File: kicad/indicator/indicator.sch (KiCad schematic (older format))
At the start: 9 parts, among them J1 Conn_01x03, Q1 2N3904, Q2 2N3904

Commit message: add pcb
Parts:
- D1, D2, D3, D4: footprint (none) -> LED_THT:LED_D3.0mm
- J1: footprint (none) -> Connector_PinSocket_2.54mm:PinSocket_1x03_P2.54mm_Vertical
- R1, R2: footprint (none) -> Resistor_SMD:R_0805_2012Metric_Pad1.20x1.40mm_HandSolder
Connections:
- net VCC: now also D1.2 (A); no longer D1.1 (K)
- net at D2.1 (K): now also D3.2 (A); no longer D1.2 (A)
- net at D2.2 (A): now also D1.1 (K); no longer D3.1 (K)
- net at D4.1 (K): now also Q2.3 (C); no longer D3.2 (A)
- net at D4.2 (A): now also D3.1 (K); no longer Q2.3 (C)
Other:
- moved on the sheet: D1, D2, D3, D4
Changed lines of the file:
@@
 F 0 "D1" V 5447 2430 50  0000 L CNN
 F 1 "LED" V 5538 2430 50  0000 L CNN
-F 2 "" H 5500 2350 50  0001 C CNN
+F 2 "LED_THT:LED_D3.0mm" H 5500 2350 50  0001 C CNN
 F 3 "~" H 5500 2350 50  0001 C CNN
 	1    5500 2350
-	0    1    1    0
+	0    -1   -1   0
 $EndComp
 $Comp
@@
 F 0 "D2" V 5447 2830 50  0000 L CNN
 F 1 "LED" V 5538 2830 50  0000 L CNN
-F 2 "" H 5500 2750 50  0001 C CNN
+F 2 "LED_THT:LED_D3.0mm" H 5500 2750 50  0001 C CNN
 F 3 "~" H 5500 2750 50  0001 C CNN
 	1    5500 2750
-	0    1    1    0
+	0    -1   -1   0
 $EndComp
 $Comp
@@
 F 0 "D3" V 5447 3230 50  0000 L CNN
 F 1 "LED" V 5538 3230 50  0000 L CNN
-F 2 "" H 5500 3150 50  0001 C CNN
+F 2 "LED_THT:LED_D3.0mm" H 5500 3150 50  0001 C CNN
 F 3 "~" H 5500 3150 50  0001 C CNN
 	1    5500 3150
-	0    1    1    0
+	0    -1   -1   0
 $EndComp
 $Comp
@@
 F 0 "D4" V 5447 3630 50  0000 L CNN
 F 1 "LED" V 5538 3630 50  0000 L CNN
-F 2 "" H 5500 3550 50  0001 C CNN
+F 2 "LED_THT:LED_D3.0mm" H 5500 3550 50  0001 C CNN
 F 3 "~" H 5500 3550 50  0001 C CNN
 	1    5500 3550
-	0    1    1    0
+	0    -1   -1   0
 $EndComp
 $Comp
@@
 F 0 "R2" H 5570 4846 50  0000 L CNN
 F 1 "R" H 5570 4755 50  0000 L CNN
-F 2 "" V 5430 4800 50  0001 C CNN
+F 2 "Resistor_SMD:R_0805_2012Metric_Pad1.20x1.40mm_HandSolder" V 5430 4800 50  0001 C CNN
 F 3 "~" H 5500 4800 50  0001 C CNN
 	1    5500 4800
@@
 F 0 "R1" V 4493 4000 50  0000 C CNN
 F 1 "R" V 4584 4000 50  0000 C CNN
-F 2 "" V 4630 4000 50  0001 C CNN
+F 2 "Resistor_SMD:R_0805_2012Metric_Pad1.20x1.40mm_HandSolder" V 4630 4000 50  0001 C CNN
 F 3 "~" H 4700 4000 50  0001 C CNN
 	1    4700 4000
@@
 F 0 "J1" H 4780 3092 50  0000 L CNN
 F 1 "Conn_01x03" H 4780 3001 50  0000 L CNN
-F 2 "" H 4700 3050 50  0001 C CNN
+F 2 "Connector_PinSocket_2.54mm:PinSocket_1x03_P2.54mm_Vertical" H 4700 3050 50  0001 C CNN
 F 3 "~" H 4700 3050 50  0001 C CNN
 	1    4700 3050
@@
 	4200 4000 4550 4000
 $Comp
-L power:VCC #PWR?
+L power:VCC #PWR0101
 U 1 1 5F767479
 P 4400 2950
-F 0 "#PWR?" H 4400 2800 50  0001 C CNN
+F 0 "#PWR0101" H 4400 2800 50  0001 C CNN
 F 1 "VCC" H 4415 3123 50  0000 C CNN
 F 2 "" H 4400 2950 50  0001 C CNN

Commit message: Add updated design
should work with the drill i've
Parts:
- D1, D2, D3, D4: footprint LED_THT:LED_D3.0mm -> indicator:LED_D3.0mm_Large_Pad
- J1: footprint Connector_PinSocket_2.54mm:PinSocket_1x03_P2.54mm_Vertical -> indicator:PinSocket_1x03_P2.54mm_Vertical_Large_Pad
- Q1, Q2: footprint Package_TO_SOT_THT:TO-92_Inline -> Package_TO_SOT_THT:TO-92_HandSolder
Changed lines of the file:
@@
 F 0 "D1" V 5447 2430 50  0000 L CNN
 F 1 "LED" V 5538 2430 50  0000 L CNN
-F 2 "LED_THT:LED_D3.0mm" H 5500 2350 50  0001 C CNN
+F 2 "indicator:LED_D3.0mm_Large_Pad" H 5500 2350 50  0001 C CNN
 F 3 "~" H 5500 2350 50  0001 C CNN
 	1    5500 2350
@@
 F 0 "D2" V 5447 2830 50  0000 L CNN
 F 1 "LED" V 5538 2830 50  0000 L CNN
-F 2 "LED_THT:LED_D3.0mm" H 5500 2750 50  0001 C CNN
+F 2 "indicator:LED_D3.0mm_Large_Pad" H 5500 2750 50  0001 C CNN
 F 3 "~" H 5500 2750 50  0001 C CNN
 	1    5500 2750
@@
 F 0 "D3" V 5447 3230 50  0000 L CNN
 F 1 "LED" V 5538 3230 50  0000 L CNN
-F 2 "LED_THT:LED_D3.0mm" H 5500 3150 50  0001 C CNN
+F 2 "indicator:LED_D3.0mm_Large_Pad" H 5500 3150 50  0001 C CNN
 F 3 "~" H 5500 3150 50  0001 C CNN
 	1    5500 3150
@@
 F 0 "D4" V 5447 3630 50  0000 L CNN
 F 1 "LED" V 5538 3630 50  0000 L CNN
-F 2 "LED_THT:LED_D3.0mm" H 5500 3550 50  0001 C CNN
+F 2 "indicator:LED_D3.0mm_Large_Pad" H 5500 3550 50  0001 C CNN
 F 3 "~" H 5500 3550 50  0001 C CNN
 	1    5500 3550
@@
 F 0 "Q2" H 5590 4046 50  0000 L CNN
 F 1 "2N3904" H 5590 3955 50  0000 L CNN
-F 2 "Package_TO_SOT_THT:TO-92_Inline" H 5600 3925 50  0001 L CIN
+F 2 "Package_TO_SOT_THT:TO-92_HandSolder" H 5600 3925 50  0001 L CIN
 F 3 "https://www.fairchildsemi.com/datasheets/2N/2N3904.pdf" H 5400 4000 50  0001 L CNN
 	1    5400 4000
@@
 F 0 "Q1" H 5291 4496 50  0000 L CNN
 F 1 "2N3904" H 5291 4405 50  0000 L CNN
-F 2 "Package_TO_SOT_THT:TO-92_Inline" H 5300 4375 50  0001 L CIN
+F 2 "Package_TO_SOT_THT:TO-92_HandSolder" H 5300 4375 50  0001 L CIN
 F 3 "https://www.fairchildsemi.com/datasheets/2N/2N3904.pdf" H 5100 4450 50  0001 L CNN
 	1    5100 4450
@@
 F 0 "J1" H 4780 3092 50  0000 L CNN
 F 1 "Conn_01x03" H 4780 3001 50  0000 L CNN
-F 2 "Connector_PinSocket_2.54mm:PinSocket_1x03_P2.54mm_Vertical" H 4700 3050 50  0001 C CNN
+F 2 "indicator:PinSocket_1x03_P2.54mm_Vertical_Large_Pad" H 4700 3050 50  0001 C CNN
 F 3 "~" H 4700 3050 50  0001 C CNN
 	1    4700 3050

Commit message: add footprint for bjts
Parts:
- Q1, Q2: footprint Package_TO_SOT_THT:TO-92_HandSolder -> indicator:TO-92_HandSolder_Large_Pad
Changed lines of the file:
@@
 F 0 "Q2" H 5590 4046 50  0000 L CNN
 F 1 "2N3904" H 5590 3955 50  0000 L CNN
-F 2 "Package_TO_SOT_THT:TO-92_HandSolder" H 5600 3925 50  0001 L CIN
+F 2 "indicator:TO-92_HandSolder_Large_Pad" H 5600 3925 50  0001 L CIN
 F 3 "https://www.fairchildsemi.com/datasheets/2N/2N3904.pdf" H 5400 4000 50  0001 L CNN
 	1    5400 4000
@@
 F 0 "Q1" H 5291 4496 50  0000 L CNN
 F 1 "2N3904" H 5291 4405 50  0000 L CNN
-F 2 "Package_TO_SOT_THT:TO-92_HandSolder" H 5300 4375 50  0001 L CIN
+F 2 "indicator:TO-92_HandSolder_Large_Pad" H 5300 4375 50  0001 L CIN
 F 3 "https://www.fairchildsemi.com/datasheets/2N/2N3904.pdf" H 5100 4450 50  0001 L CNN
 	1    5100 4450

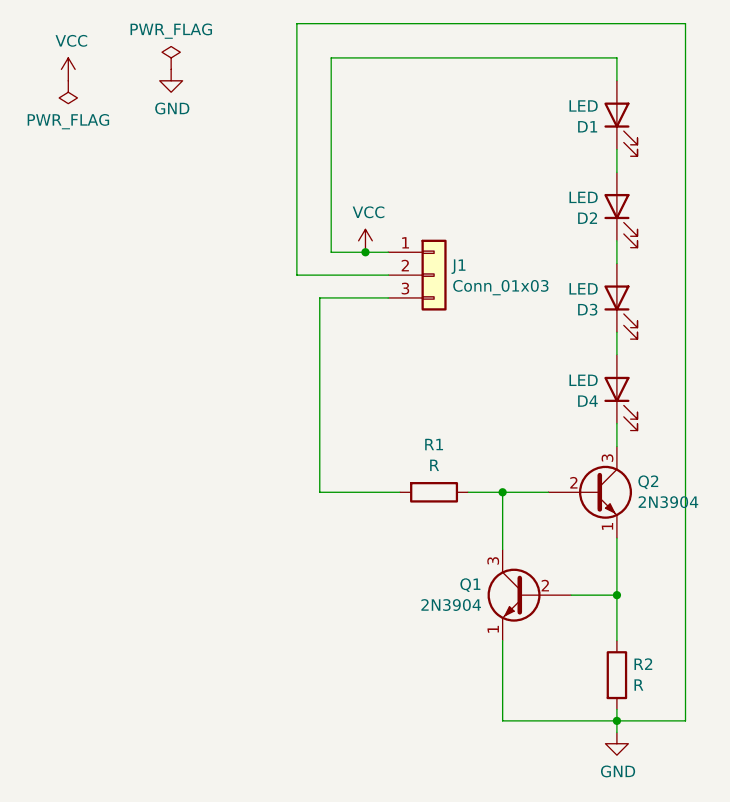
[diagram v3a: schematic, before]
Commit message: Add resistors values
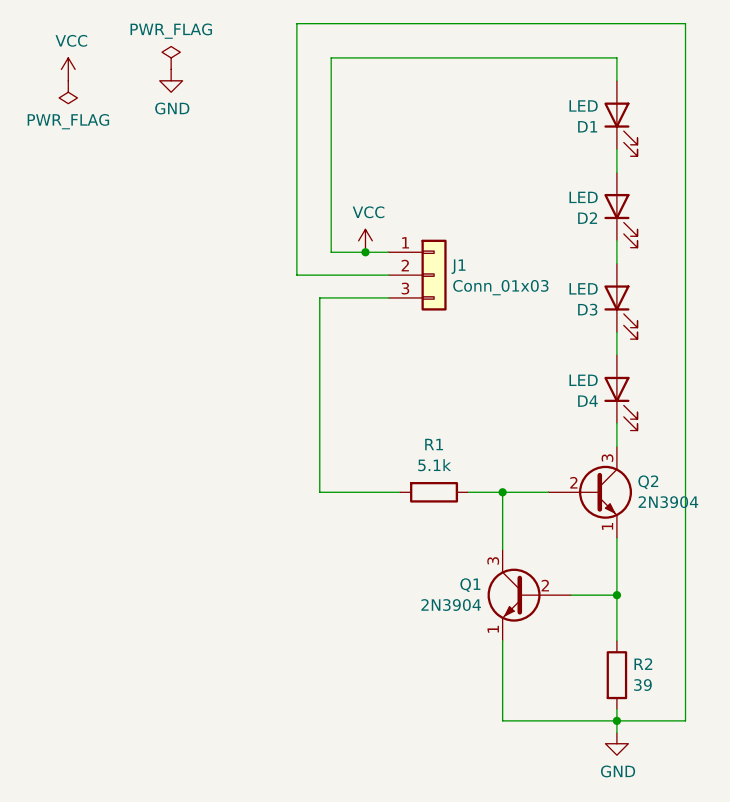
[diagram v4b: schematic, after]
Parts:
- R1: value R -> 5.1k
- R2: value R -> 39
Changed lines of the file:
@@
 P 5500 4800
 F 0 "R2" H 5570 4846 50  0000 L CNN
-F 1 "R" H 5570 4755 50  0000 L CNN
+F 1 "39" H 5570 4755 50  0000 L CNN
 F 2 "Resistor_SMD:R_0805_2012Metric_Pad1.20x1.40mm_HandSolder" V 5430 4800 50  0001 C CNN
 F 3 "~" H 5500 4800 50  0001 C CNN
@@
 P 4700 4000
 F 0 "R1" V 4493 4000 50  0000 C CNN
-F 1 "R" V 4584 4000 50  0000 C CNN
+F 1 "5.1k" V 4584 4000 50  0000 C CNN
 F 2 "Resistor_SMD:R_0805_2012Metric_Pad1.20x1.40mm_HandSolder" V 4630 4000 50  0001 C CNN
 F 3 "~" H 4700 4000 50  0001 C CNN
